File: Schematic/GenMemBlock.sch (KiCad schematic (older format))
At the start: 30 parts, among them J1 MCU_HEADER, J2 ADDR_BUS, J3 DATA_BUS, J4 CART_A20, J5 CART_B10, J6 CART_B20, J7 CART_A10, U1 74HCT595, U10 74ACT16543DL, U2 74HCT595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

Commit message: working version v3
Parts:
- added J8: Conn_02x04_Odd_Even, Connector_PinHeader_2.54mm:PinHeader_2x04_P2.54mm_Vertical, symbol Connector_Generic:Conn_02x04_Odd_Even
- added P1: MD-CART-FINGERS-doragasu, md-fingers:md-cart, symbol md-cart:MD-CART-FINGERS-doragasu
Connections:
- net labels added: DTACK#, H_RESET#, RESET#, S_RESET#
- net labels removed: GEN_DTACK#
- wire segments 412 -> 483
- no-connect marks 33 -> 44
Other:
- moved on the sheet: R3

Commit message: read/write gencart, removed reset header and use H_RESET#
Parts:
- removed J8: Conn_02x04_Odd_Even, Connector_PinHeader_2.54mm:PinHeader_2x04_P2.54mm_Vertical, symbol Connector_Generic:Conn_02x04_Odd_Even
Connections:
- net labels added: GEN_WE#
- net labels removed: DO_OE
- wire segments 483 -> 473
- no-connect marks 44 -> 41
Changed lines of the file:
@@
 GND
 Text Label 2600 3600 0    50   ~ 0
-VCC
+GEN_CE#
 Text Label 700  3700 0    50   ~ 0
 GND
@@
 GND
 Text Label 2600 1100 0    50   ~ 0
-GND
+GEN_WE#
 Entry Wire Line
 	2750 1100 2850 1000
@@
 	2750 3800 2850 3700
 Text Label 700  1100 0    50   ~ 0
-DO_OE
+GEN_OE#
 Text Label 2600 1200 0    50   ~ 0
 GND
@@
 GND
 Text Label 700  3600 0    50   ~ 0
-GND
+GEN_CE#
 Text Label 2600 3700 0    50   ~ 0
 GND
@@
 Text GLabel 10250 5750 2    50   Input ~ 0
 ROM_CE#
-NoConn ~ 10250 5850
 Text GLabel 10250 6050 2    50   Input ~ 0
 GEN_RESET#
@@
 	10300 3200 10400 3100
 NoConn ~ 9950 3650
-NoConn ~ 10050 3650
 NoConn ~ 9950 4150
 NoConn ~ 10050 4150
@@
 Text Label 9350 4450 0    50   ~ 0
 CTRL_OE
-Text Label 9350 4250 0    50   ~ 0
-DO_OE
 Text GLabel 9300 4450 0    50   Input ~ 0
 TX_ENABLE#
 Text Label 2600 3800 0    50   ~ 0
-GND
+GEN_WE#
 Text Label 700  3800 0    50   ~ 0
-DO_OE
+GEN_OE#
 Text Label 700  1300 0    50   ~ 0
-GND
+GEN_CE#
 Text Label 2600 1300 0    50   ~ 0
-VCC
+GEN_CE#
 $Comp
 L Connector_Generic:Conn_02x10_Odd_Even J6
@@
 GND
 Text Label 7500 2700 0    50   ~ 0
-VCC
+GEN_WE#
 $Comp
 L power:GND #PWR0114
@@
 Text Label 14300 4800 0    50   ~ 0
 GEN_OE#
-NoConn ~ 14250 5000
 NoConn ~ 14250 5100
 NoConn ~ 14250 5200
@@
 Text Label 10850 4600 1    50   ~ 0
 S_RESET#
-$Comp
-L Connector_Generic:Conn_02x04_Odd_Even J8
-U 1 1 620DA531
-P 13450 5750
-F 0 "J8" H 13500 6067 50  0000 C CNN
-F 1 "Conn_02x04_Odd_Even" H 13500 5976 50  0000 C CNN
-F 2 "Connector_PinHeader_2.54mm:PinHeader_2x04_P2.54mm_Vertical" H 13450 5750 50  0001 C CNN
-F 3 "~" H 13450 5750 50  0001 C CNN
-	1    13450 5750
-	1    0    0    -1
-$EndComp
-Wire Wire Line
-	13250 5950 13150 5950
-Wire Wire Line
-	13150 5950 13150 5850
-Wire Wire Line
-	13250 5750 13150 5750
-Wire Wire Line
-	13250 5850 13150 5850
-Connection ~ 13150 5850
-Wire Wire Line
-	13150 5850 13150 5750
-Wire Wire Line
-	13150 5750 13050 5750
-Connection ~ 13150 5750
-Text GLabel 13050 5750 0    50   Input ~ 0
+Text GLabel 13750 5850 0    50   Input ~ 0
 GEN_RESET#
-Wire Wire Line
-	13750 5950 14150 5950
-Text Label 13750 5950 0    50   ~ 0
-S_RESET#
 Text Label 13750 5850 0    50   ~ 0
 H_RESET#
-Text Label 13750 5750 0    50   ~ 0
-RESET#
-Wire Wire Line
-	13750 5650 14150 5650
-Wire Wire Line
-	13750 5750 14150 5750
 Wire Wire Line
 	13750 5850 14150 5850
-Entry Wire Line
-	14150 5950 14250 6050
-Entry Wire Line
-	14150 5850 14250 5950
-Entry Wire Line
-	14150 5750 14250 5850
-Entry Wire Line
-	14150 5650 14250 5750
 Wire Bus Line
 	14250 5550 15000 5550
-Text Label 13750 5650 0    50   ~ 0
-DTACK#
-Wire Wire Line
-	13250 5650 12850 5650
-$Comp
-L power:+5V #PWR0101
-U 1 1 626A5866
-P 12850 5650
-F 0 "#PWR0101" H 12850 5500 50  0001 C CNN
-F 1 "+5V" H 12865 5823 50  0000 C CNN
-F 2 "" H 12850 5650 50  0001 C CNN
-F 3 "" H 12850 5650 50  0001 C CNN
-	1    12850 5650
-	1    0    0    -1
-$EndComp
 $Comp
 L power:+5V #PWR0116
@@
 	9750 4350 9850 4450
 Entry Wire Line
-	9750 4250 9850 4350
-Entry Wire Line
-	9750 4150 9850 4250
+	14900 5000 15000 5100
 Wire Wire Line
-	9750 4150 9300 4150
+	14900 5000 14250 5000
+Text Label 14300 5000 0    50   ~ 0
+GEN_WE#
+Entry Wire Line
+	10050 3300 10150 3200
 Wire Wire Line
-	9300 4150 9300 4250
+	10050 3300 10050 3650
+Text Label 10050 3650 1    50   ~ 0
+GEN_WE#
+Entry Wire Line
+	14150 5850 14250 5950
+Text GLabel 10250 5850 2    50   Input ~ 0
+DTACK#
+Entry Wire Line
+	14150 5650 14250 5750
+Text GLabel 13750 5650 0    50   Input ~ 0
+DTACK#
 Wire Wire Line
-	9300 4250 9750 4250
+	13750 5650 14150 5650
 Wire Bus Line
 	5950 6450 7300 6450
@@
 	11050 5150 11050 6150
 Wire Bus Line
+	9850 3200 9850 4600
+Wire Bus Line
+	14250 5550 14250 6050
+Wire Bus Line
 	9850 4600 10450 4600
 Wire Bus Line
@@
 	2550 4550 2550 5650
 Wire Bus Line
-	14250 5550 14250 6050
-Wire Bus Line
 	11950 100  11950 4500
 Wire Bus Line
@@
 	3350 5650 3350 6650
 Wire Bus Line
-	9850 3200 9850 4600
-Wire Bus Line
 	9850 3200 10700 3200
 Wire Bus Line
@@
 Wire Bus Line
 	15000 100  15000 5550
-Text Label 9350 4150 0    50   ~ 0
-GEN_CE#
+Text Label 13750 5650 0    50   ~ 0
+DTACK#
 $EndSCHEMATC

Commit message: sega/microcontroller interop
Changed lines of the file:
@@
 $Descr A4 11693 8268
 encoding utf-8
-Sheet 1 1
+Sheet 1 2
 Title ""
 Date ""
@@
 Wire Wire Line
 	13750 5650 14150 5650
+Text Label 13750 5650 0    50   ~ 0
+DTACK#
 Wire Bus Line
 	5950 6450 7300 6450
@@
 Wire Bus Line
 	15000 100  15000 5550
-Text Label 13750 5650 0    50   ~ 0
-DTACK#
+$Sheet
+S 12450 6950 650  150
+U 65320705
+F0 "Mem Module" 50
+F1 "mem_module.sch" 50
+$EndSheet
 $EndSCHEMATC

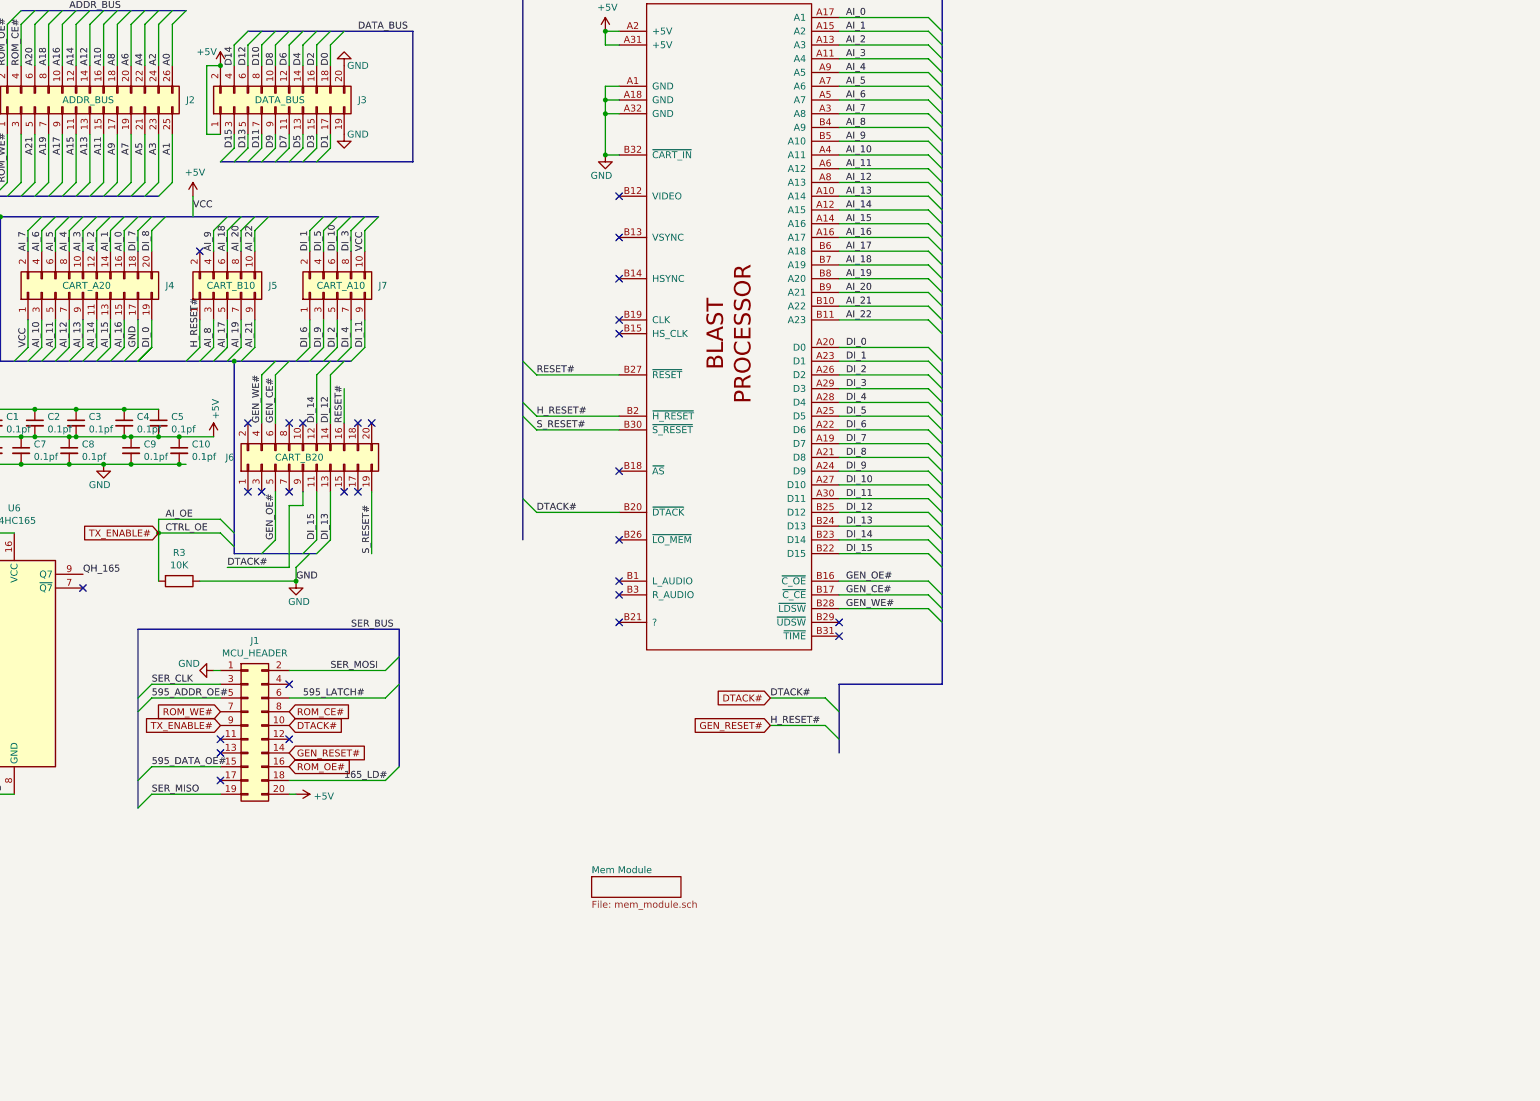
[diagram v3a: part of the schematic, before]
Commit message: isolated common logic chips from mc board
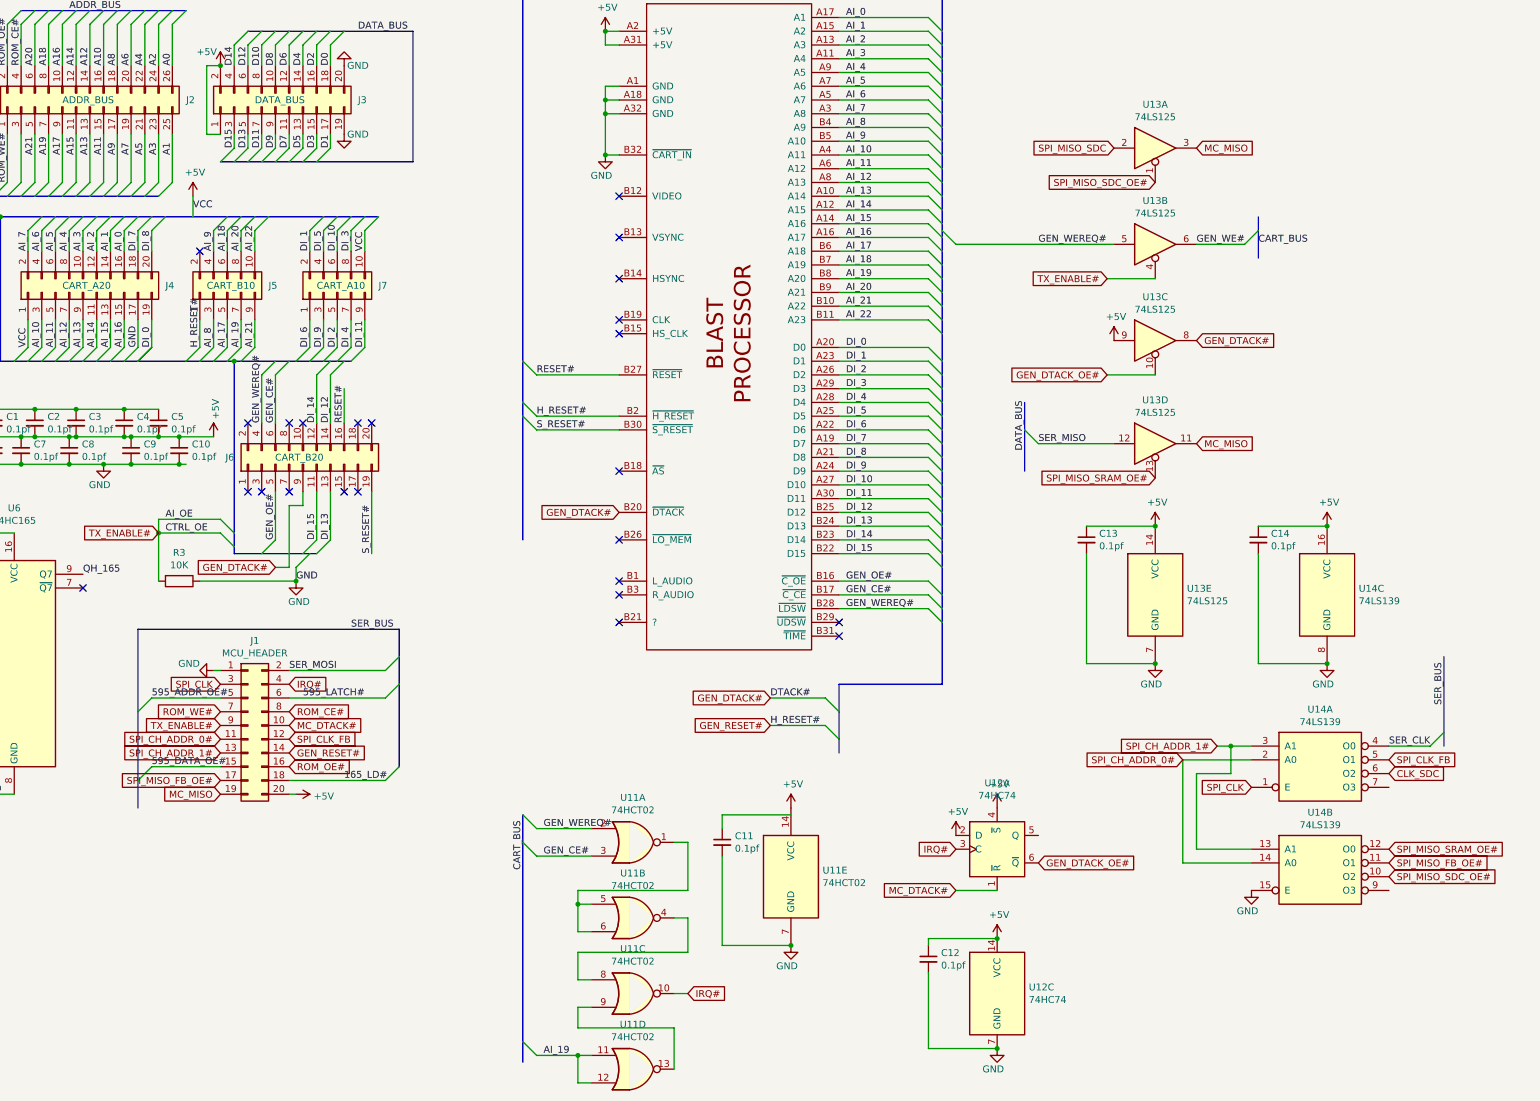
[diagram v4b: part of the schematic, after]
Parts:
- added C11, C12, C13, C14: 0.1pf, Capacitor_SMD:C_0805_2012Metric_Pad1.18x1.45mm_HandSolder, symbol Device:C_Small
- added U11: 74HCT02, Package_SO:TSSOP-14_4.4x5mm_P0.65mm, symbol 74xx:74HCT02
- added U12: 74HC74, Package_SO:TSSOP-14_4.4x5mm_P0.65mm, symbol 74xx:74HC74
- added U13: 74LS125, Package_SO:TSSOP-14_4.4x5mm_P0.65mm, symbol 74xx:74LS125
- added U14: 74LS139, Package_SO:TSSOP-16_4.4x5mm_P0.65mm, symbol 74xx:74LS139
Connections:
- net +5V: now also C12.1, C13.1, C14.1, U11.14 (VCC), U12.14 (VCC), U12.2 (D), U12.4 (~S), U13.14 (VCC), U13.9, U14.16 (VCC)
- net AI_19: now also U11.11, U11.12
- net GEN_CE#: now also U11.3
- net GEN_WE#: now also U13.6; no longer J6.4 (Pin_4), P1.B28 (~LDSW)
- net GND: now also C11.2, C12.2, C13.2, C14.2, U11.7 (GND), U12.7 (GND), U13.7 (GND), U14.15 (E), U14.8 (GND)
- net SER_CLK: now also U14.4 (O0); no longer J1.3 (Pin_3)
- net SER_MISO: now also U13.12; no longer J1.19 (Pin_19)
- net TX_ENABLE#: now also U13.4
- net SPI_CH_ADDR_0#: now reaches J1.11 (Pin_11)
- net SPI_CH_ADDR_0#: now also U14.14 (A0), U14.2 (A0)
- net SPI_CLK_FB: now reaches J1.12 (Pin_12)
- net SPI_CLK_FB: now also U14.5 (O1)
- net SPI_CH_ADDR_1#: now reaches J1.13 (Pin_13)
- net SPI_CH_ADDR_1#: now also U14.13 (A1), U14.3 (A1)
- net SPI_MISO_FB_OE#: now reaches J1.17 (Pin_17)
- net SPI_MISO_FB_OE#: now also U14.11 (O1)
- net IRQ#: now reaches J1.4 (Pin_4)
- net IRQ#: now also U11.10, U12.3 (C)
- net DTACK# renamed GEN_DTACK#
- net GEN_DTACK#: now also U13.8; no longer J1.10 (Pin_10)
- new net: U11.1, U11.5, U11.6
- new net: U11.4, U11.8
- new net: U11.13, U11.9
- new net CLK_SDC: U14.6 (O2)
- new net GEN_DTACK_OE#: U12.6 (~Q), U13.10
- new net GEN_WEREQ#: J6.4 (Pin_4), P1.B28 (~LDSW), U11.2, U13.5
- new net MC_DTACK#: J1.10 (Pin_10), U12.1 (~R)
- new net MC_MISO: J1.19 (Pin_19), U13.11, U13.3
- new net SPI_CLK: J1.3 (Pin_3), U14.1 (E)
- new net SPI_MISO_SDC: U13.2
- new net SPI_MISO_SDC_OE#: U13.1, U14.10 (O2)
- new net SPI_MISO_SRAM_OE#: U13.13, U14.12 (O0)
- no-connect marks 41 -> 36

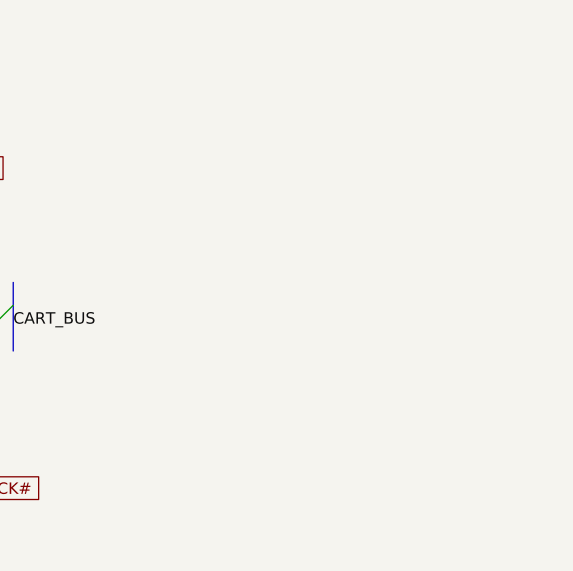
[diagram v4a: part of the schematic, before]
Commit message: sdcard wiring
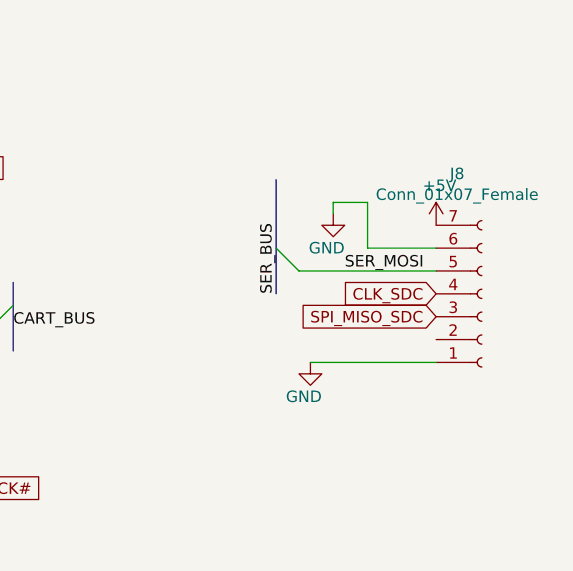
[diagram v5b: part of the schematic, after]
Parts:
- added J8: Conn_01x07_Female, Connector_PinHeader_2.54mm:PinHeader_1x07_P2.54mm_Vertical, symbol Connector:Conn_01x07_Female
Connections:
- net +5V: now also J8.7 (Pin_7)
- net CLK_SDC: now also J8.4 (Pin_4)
- net GND: now also J8.1 (Pin_1), J8.6 (Pin_6)
- net SER_MOSI: now also J8.5 (Pin_5)
- net SPI_MISO_SDC: now also J8.3 (Pin_3)
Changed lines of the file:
@@
 Text Label 10250 5450 0    50   ~ 0
 SER_MOSI
+Text GLabel 9750 6350 0    50   Input ~ 0
+MC_MISO
+$Comp
+L power:GND #PWR0129
+U 1 1 6696674C
+P 18600 2500
+F 0 "#PWR0129" H 18600 2250 50  0001 C CNN
+F 1 "GND" H 18650 2350 50  0000 R CNN
+F 2 "" H 18600 2500 50  0001 C CNN
+F 3 "" H 18600 2500 50  0001 C CNN
+	1    18600 2500
+	1    0    0    -1
+$EndComp
+Wire Wire Line
+	18600 2500 19150 2500
+Text GLabel 19150 2300 0    50   Input ~ 0
+SPI_MISO_SDC
+Text GLabel 19150 2200 0    50   Input ~ 0
+CLK_SDC
+$Comp
+L Connector:Conn_01x07_Female J8
+U 1 1 6696020D
+P 19350 2200
+F 0 "J8" H 19242 1675 50  0000 C CNN
+F 1 "Conn_01x07_Female" H 19242 1766 50  0000 C CNN
+F 2 "Connector_PinHeader_2.54mm:PinHeader_1x07_P2.54mm_Vertical" H 19350 2200 50  0001 C CNN
+F 3 "~" H 19350 2200 50  0001 C CNN
+	1    19350 2200
+	1    0    0    1
+$EndComp
+Wire Wire Line
+	19150 2100 18550 2100
+Text Label 18450 2200 1    50   ~ 0
+SER_BUS
+Entry Wire Line
+	18450 2000 18550 2100
+Text Label 18750 2100 0    50   ~ 0
+SER_MOSI
+$Comp
+L power:+5V #PWR?
+U 1 1 66EC71D7
+P 19150 1900
+F 0 "#PWR?" H 19150 1750 50  0001 C CNN
+F 1 "+5V" H 19165 2073 50  0000 C CNN
+F 2 "" H 19150 1900 50  0001 C CNN
+F 3 "" H 19150 1900 50  0001 C CNN
+	1    19150 1900
+	1    0    0    -1
+$EndComp
+$Comp
+L power:GND #PWR?
+U 1 1 66EC7B5B
+P 18700 1850
+F 0 "#PWR?" H 18700 1600 50  0001 C CNN
+F 1 "GND" H 18750 1700 50  0000 R CNN
+F 2 "" H 18700 1850 50  0001 C CNN
+F 3 "" H 18700 1850 50  0001 C CNN
+	1    18700 1850
+	1    0    0    -1
+$EndComp
+Wire Wire Line
+	19150 2000 18850 2000
+Wire Wire Line
+	18850 2000 18850 1800
+Wire Wire Line
+	18850 1800 18700 1800
+Wire Wire Line
+	18700 1800 18700 1850
+Wire Bus Line
+	18450 1700 18450 2200
 Wire Bus Line
 	15600 3500 15600 4000
@@
 Wire Bus Line
 	15000 100  15000 5550
-Text GLabel 9750 6350 0    50   Input ~ 0
-MC_MISO
 $EndSCHEMATC

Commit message: moved to single board with SPI splitter
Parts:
- added R4: 10K, Resistor_SMD:R_0805_2012Metric_Pad1.20x1.40mm_HandSolder, symbol Device:R
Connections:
- net +5V: now also C11.1, R4.2
- net GEN_WE#: now also R4.1
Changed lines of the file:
@@
 $EndComp
 Wire Wire Line
-	13900 6500 13400 6500
-Wire Wire Line
-	13400 6500 13400 6600
+	13900 6450 13400 6450
+Wire Wire Line
+	13400 6450 13400 6600
 Wire Wire Line
 	13400 6800 13400 7450
@@
 SER_MOSI
 $Comp
-L power:+5V #PWR?
+L power:+5V #PWR0130
 U 1 1 66EC71D7
 P 19150 1900
-F 0 "#PWR?" H 19150 1750 50  0001 C CNN
+F 0 "#PWR0130" H 19150 1750 50  0001 C CNN
 F 1 "+5V" H 19165 2073 50  0000 C CNN
 F 2 "" H 19150 1900 50  0001 C CNN
@@
 $EndComp
 $Comp
-L power:GND #PWR?
+L power:GND #PWR0131
 U 1 1 66EC7B5B
 P 18700 1850
-F 0 "#PWR?" H 18700 1600 50  0001 C CNN
+F 0 "#PWR0131" H 18700 1600 50  0001 C CNN
 F 1 "GND" H 18750 1700 50  0000 R CNN
 F 2 "" H 18700 1850 50  0001 C CNN
@@
 Wire Wire Line
 	18700 1800 18700 1850
+$Comp
+L Device:R R4
+U 1 1 656B7B44
+P 17200 2100
+F 0 "R4" V 16993 2100 50  0000 C CNN
+F 1 "10K" V 17084 2100 50  0000 C CNN
+F 2 "Resistor_SMD:R_0805_2012Metric_Pad1.20x1.40mm_HandSolder" V 17130 2100 50  0001 C CNN
+F 3 "~" H 17200 2100 50  0001 C CNN
+	1    17200 2100
+	-1   0    0    1
+$EndComp
+Wire Wire Line
+	17200 2350 17200 2250
+$Comp
+L power:+5V #PWR0132
+U 1 1 65719933
+P 17200 1950
+F 0 "#PWR0132" H 17200 1800 50  0001 C CNN
+F 1 "+5V" H 17215 2123 50  0000 C CNN
+F 2 "" H 17200 1950 50  0001 C CNN
+F 3 "" H 17200 1950 50  0001 C CNN
+	1    17200 1950
+	1    0    0    -1
+$EndComp
 Wire Bus Line
 	18450 1700 18450 2200
@@
 Wire Bus Line
 	15000 100  15000 5550
+Connection ~ 13900 6450
 $EndSCHEMATC
